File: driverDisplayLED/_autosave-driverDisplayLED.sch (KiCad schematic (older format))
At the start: 70 parts, among them J1 Conn_01x12_Male, J10 Conn_01x12_Male, J11 Conn_01x12_Male, J12 Conn_01x12_Male, J13 Conn_01x12_Male, J14 Conn_01x12_Male, J15 Conn_01x12_Male, J16 Conn_01x12_Male, J17 Conn_01x12_Male, J18 Conn_02x08_Counter_Clockwise, J2 Conn_01x12_Male, J3 Conn_01x12_Male, J4 Conn_02x08_Counter_Clockwise, J5 Conn_01x12_Male, J6 Conn_01x12_Male, J7 Conn_01x12_Male, J8 Conn_01x12_Male, J9 Conn_01x12_Male, Q1 FDS4953, Q2 FDS4953, Q3 FDS4953, Q4 FDS4953, Q5 FDS4953, Q6 FDS4953, Q7 FDS4953, Q8 FDS4953, U1 74HC245, U10 74HC595, U11 74HC595, U12 74HC595, U13 74HC595, U2 74HC595, U3 74HC595, U4 74HC245, U5 74HC138D, U6 74HC04, U7 74HC595, U8 74HC595, U9 74HC138D

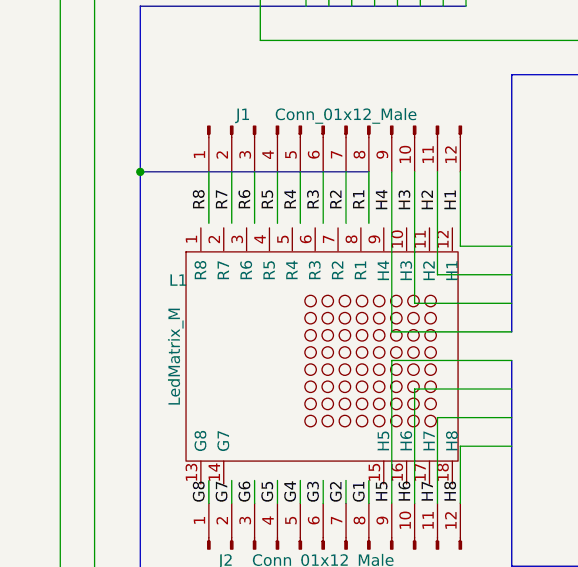
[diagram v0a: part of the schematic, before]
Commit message: place components into PCB
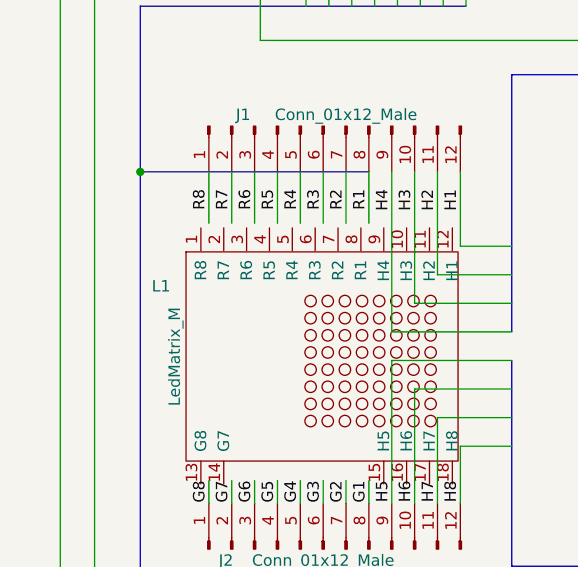
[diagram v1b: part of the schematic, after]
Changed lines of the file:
@@
 	0    -1   -1   0
-$EndComp
-$Comp
-L myLedMatrix:LedMatrix_M L1
-U 1 1 5FAA9D97
-P 1850 3975
-F 0 "L1" H 1325 4300 50  0000 L CNN
-F 1 "LedMatrix_M" V 1350 3750 50  0000 L CNN
-F 2 "" H 1950 4450 50  0001 C CNN
-F 3 "" H 1950 4450 50  0001 C CNN
-	1    1850 3975
-	1    0    0    -1
 $EndComp
 Text Label 1500 3250 3    50   ~ 0
@@
 Wire Bus Line
 	7525 2450 7950 2450
+$Comp
+L myLedMatrix:LedMatrix_M L1
+U 1 1 5FAA9D97
+P 1850 3975
+F 0 "L1" H 1250 4275 50  0000 L CNN
+F 1 "LedMatrix_M" V 1350 3750 50  0000 L CNN
+F 2 "" H 1950 4450 50  0001 C CNN
+F 3 "" H 1950 4450 50  0001 C CNN
+	1    1850 3975
+	1    0    0    -1
+$EndComp
 $EndSCHEMATC
